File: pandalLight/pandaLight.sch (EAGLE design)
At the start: 110 parts, among them J1 PJ-037A, U13 TPD12S016PWR, U15 PMOD-2X6, U16 PMOD-2X6, U17 PLR135-T10, U18 PLT133-T10W, U20 TP10SQ, U21 TP10SQ, U22 PAN1322, U23 6SLX9TQG144, U4 FT2232HL, U5 93LC46BT-I/OT, U6 51, U7 51, U8 TPD12S016PWR, X1 USBUB-S, X2 HDMI_RECEPTICAL_A, X4 HDMI_RECEPTICAL_A, Y1 403, Y2 20Mhz

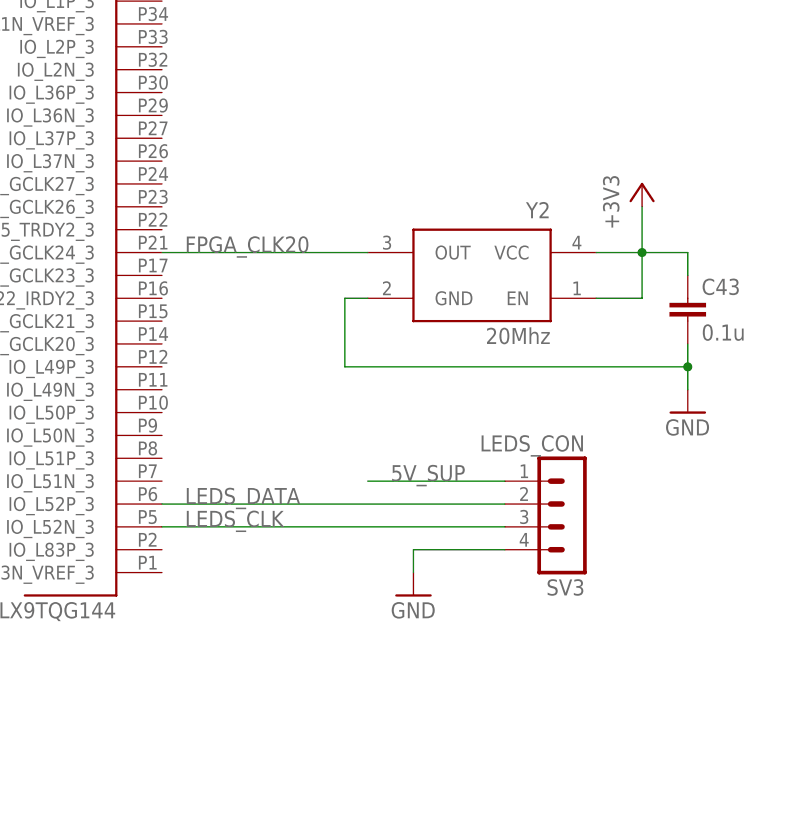
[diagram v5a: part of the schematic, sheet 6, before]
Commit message: Minor library changes; Searching for CMOS to TTL level shifters for the LED strip outputs
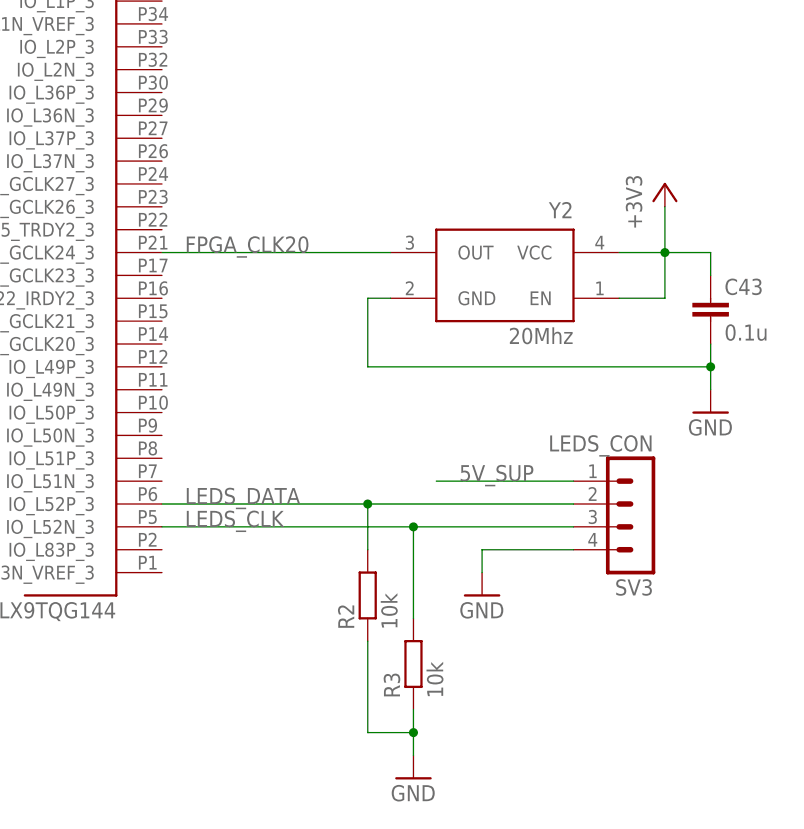
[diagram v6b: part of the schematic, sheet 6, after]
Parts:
- added R2, R3: 10k, pandaLight:RESISTOR0402
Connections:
- net GND: now also R2.1, R3.1
- net LEDS_CLK: now also R3.2
- net LEDS_DATA: now also R2.2
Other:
- moved on the sheet: C43, SV3, Y2
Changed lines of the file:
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@@
 <part name="GND7" library="pandaLight" deviceset="GND" device=""/>
 <part name="GND10" library="pandaLight" deviceset="GND" device=""/>
+<part name="R2" library="pandaLight" deviceset="RESISTOR" device="0402" value="10k"/>
+<part name="R3" library="pandaLight" deviceset="RESISTOR" device="0402" value="10k"/>
+<part name="GND16" library="pandaLight" deviceset="GND" device=""/>
 </parts>
 <sheets>
@@
 <instance part="GND46" gate="1" x="66.04" y="81.28"/>
 <instance part="U23" gate="B3" x="30.48" y="48.26"/>
-<instance part="SV3" gate="G$1" x="81.28" y="17.78" rot="R180">
-<attribute name="PARTNO" x="81.28" y="17.78" size="1.778" layer="96" display="off"/>
-<attribute name="BOM" x="81.28" y="17.78" size="1.778" layer="96" rot="R180" display="off"/>
-</instance>
-<instance part="Y2" gate="G$1" x="71.12" y="45.72" rot="MR0">
-<attribute name="PARTNO" x="71.12" y="45.72" size="1.778" layer="96" rot="MR0" display="off"/>
-</instance>
-<instance part="PS27" gate="G$1" x="88.9" y="55.88"/>
-<instance part="C43" gate="G$1" x="93.98" y="43.18">
-<attribute name="PARTNO" x="93.98" y="43.18" size="1.778" layer="96" display="off"/>
-</instance>
-<instance part="GND32" gate="1" x="93.98" y="30.48"/>
-<instance part="GND7" gate="1" x="63.5" y="10.16"/>
+<instance part="SV3" gate="G$1" x="88.9" y="17.78" rot="R180">
+<attribute name="PARTNO" x="88.9" y="17.78" size="1.778" layer="96" display="off"/>
+<attribute name="BOM" x="88.9" y="17.78" size="1.778" layer="96" rot="R180" display="off"/>
+</instance>
+<instance part="Y2" gate="G$1" x="73.66" y="45.72" rot="MR0">
+<attribute name="PARTNO" x="73.66" y="45.72" size="1.778" layer="96" rot="MR0" display="off"/>
+</instance>
+<instance part="PS27" gate="G$1" x="91.44" y="55.88"/>
+<instance part="C43" gate="G$1" x="96.52" y="43.18">
+<attribute name="PARTNO" x="96.52" y="43.18" size="1.778" layer="96" display="off"/>
+</instance>
+<instance part="GND32" gate="1" x="96.52" y="30.48"/>
+<instance part="GND7" gate="1" x="71.12" y="10.16"/>
+<instance part="R2" gate="G$1" x="58.42" y="10.16" rot="R90"/>
+<instance part="R3" gate="G$1" x="63.5" y="2.54" rot="R90"/>
+<instance part="GND16" gate="1" x="63.5" y="-10.16"/>
 </instances>
 <busses>
@@
 <pinref part="GND32" gate="1" pin="GND"/>
 <pinref part="Y2" gate="G$1" pin="GND"/>
-<wire x1="93.98" y1="35.56" x2="93.98" y2="33.02" width="0.1524" layer="91"/>
-<wire x1="58.42" y1="43.18" x2="55.88" y2="43.18" width="0.1524" layer="91"/>
-<wire x1="55.88" y1="43.18" x2="55.88" y2="35.56" width="0.1524" layer="91"/>
-<wire x1="55.88" y1="35.56" x2="93.98" y2="35.56" width="0.1524" layer="91"/>
+<wire x1="96.52" y1="35.56" x2="96.52" y2="33.02" width="0.1524" layer="91"/>
+<wire x1="60.96" y1="43.18" x2="58.42" y2="43.18" width="0.1524" layer="91"/>
+<wire x1="58.42" y1="43.18" x2="58.42" y2="35.56" width="0.1524" layer="91"/>
+<wire x1="58.42" y1="35.56" x2="96.52" y2="35.56" width="0.1524" layer="91"/>
 <pinref part="C43" gate="G$1" pin="2"/>
-<wire x1="93.98" y1="38.1" x2="93.98" y2="35.56" width="0.1524" layer="91"/>
-<junction x="93.98" y="35.56"/>
+<wire x1="96.52" y1="38.1" x2="96.52" y2="35.56" width="0.1524" layer="91"/>
+<junction x="96.52" y="35.56"/>
 </segment>
 <segment>
 <pinref part="SV3" gate="G$1" pin="4"/>
-<wire x1="73.66" y1="15.24" x2="63.5" y2="15.24" width="0.1524" layer="91"/>
-<wire x1="63.5" y1="15.24" x2="63.5" y2="12.7" width="0.1524" layer="91"/>
+<wire x1="81.28" y1="15.24" x2="71.12" y2="15.24" width="0.1524" layer="91"/>
+<wire x1="71.12" y1="15.24" x2="71.12" y2="12.7" width="0.1524" layer="91"/>
 <pinref part="GND7" gate="1" pin="GND"/>
+</segment>
+<segment>
+<pinref part="R2" gate="G$1" pin="1"/>
+<wire x1="58.42" y1="5.08" x2="58.42" y2="-5.08" width="0.1524" layer="91"/>
+<pinref part="R3" gate="G$1" pin="1"/>
+<wire x1="58.42" y1="-5.08" x2="63.5" y2="-5.08" width="0.1524" layer="91"/>
+<wire x1="63.5" y1="-5.08" x2="63.5" y2="-2.54" width="0.1524" layer="91"/>
+<pinref part="GND16" gate="1" pin="GND"/>
+<wire x1="63.5" y1="-5.08" x2="63.5" y2="-7.62" width="0.1524" layer="91"/>
+<junction x="63.5" y="-5.08"/>
 </segment>
 </net>
@@
 <pinref part="U23" gate="B3" pin="IO_L52P_3"/>
 <pinref part="SV3" gate="G$1" pin="2"/>
-<wire x1="35.56" y1="20.32" x2="73.66" y2="20.32" width="0.1524" layer="91"/>
+<wire x1="35.56" y1="20.32" x2="58.42" y2="20.32" width="0.1524" layer="91"/>
 <label x="38.1" y="20.32" size="1.778" layer="95"/>
+<pinref part="R2" gate="G$1" pin="2"/>
+<wire x1="58.42" y1="20.32" x2="81.28" y2="20.32" width="0.1524" layer="91"/>
+<wire x1="58.42" y1="20.32" x2="58.42" y2="15.24" width="0.1524" layer="91"/>
+<junction x="58.42" y="20.32"/>
 </segment>
 </net>
@@
 <pinref part="SV3" gate="G$1" pin="3"/>
 <pinref part="U23" gate="B3" pin="IO_L52N_3"/>
-<wire x1="73.66" y1="17.78" x2="35.56" y2="17.78" width="0.1524" layer="91"/>
+<wire x1="81.28" y1="17.78" x2="63.5" y2="17.78" width="0.1524" layer="91"/>
 <label x="38.1" y="17.78" size="1.778" layer="95"/>
+<wire x1="63.5" y1="17.78" x2="35.56" y2="17.78" width="0.1524" layer="91"/>
+<pinref part="R3" gate="G$1" pin="2"/>
+<wire x1="63.5" y1="17.78" x2="63.5" y2="7.62" width="0.1524" layer="91"/>
+<junction x="63.5" y="17.78"/>
 </segment>
 </net>
@@
 <pinref part="PS27" gate="G$1" pin="+3V3"/>
 <pinref part="Y2" gate="G$1" pin="VCC"/>
-<wire x1="88.9" y1="43.18" x2="88.9" y2="48.26" width="0.1524" layer="91"/>
-<wire x1="88.9" y1="48.26" x2="88.9" y2="53.34" width="0.1524" layer="91"/>
-<wire x1="83.82" y1="48.26" x2="88.9" y2="48.26" width="0.1524" layer="91"/>
-<junction x="88.9" y="48.26"/>
+<wire x1="91.44" y1="43.18" x2="91.44" y2="48.26" width="0.1524" layer="91"/>
+<wire x1="91.44" y1="48.26" x2="91.44" y2="53.34" width="0.1524" layer="91"/>
+<wire x1="86.36" y1="48.26" x2="91.44" y2="48.26" width="0.1524" layer="91"/>
+<junction x="91.44" y="48.26"/>
 <pinref part="Y2" gate="G$1" pin="EN"/>
-<wire x1="83.82" y1="43.18" x2="88.9" y2="43.18" width="0.1524" layer="91"/>
+<wire x1="86.36" y1="43.18" x2="91.44" y2="43.18" width="0.1524" layer="91"/>
 <pinref part="C43" gate="G$1" pin="1"/>
-<wire x1="88.9" y1="48.26" x2="93.98" y2="48.26" width="0.1524" layer="91"/>
-<wire x1="93.98" y1="48.26" x2="93.98" y2="45.72" width="0.1524" layer="91"/>
+<wire x1="91.44" y1="48.26" x2="96.52" y2="48.26" width="0.1524" layer="91"/>
+<wire x1="96.52" y1="48.26" x2="96.52" y2="45.72" width="0.1524" layer="91"/>
 </segment>
 </net>
@@
 <pinref part="U23" gate="B3" pin="IO_L42N_GCLK24_3"/>
 <pinref part="Y2" gate="G$1" pin="OUT"/>
-<wire x1="35.56" y1="48.26" x2="58.42" y2="48.26" width="0.1524" layer="91"/>
+<wire x1="35.56" y1="48.26" x2="60.96" y2="48.26" width="0.1524" layer="91"/>
 <label x="38.1" y="48.26" size="1.778" layer="95"/>
 </segment>
@@
 <segment>
 <pinref part="SV3" gate="G$1" pin="1"/>
-<wire x1="73.66" y1="22.86" x2="58.42" y2="22.86" width="0.1524" layer="91"/>
-<label x="60.96" y="22.86" size="1.778" layer="95"/>
-</segment>
-</net>
+<wire x1="81.28" y1="22.86" x2="66.04" y2="22.86" width="0.1524" layer="91"/>
+<label x="68.58" y="22.86" size="1.778" layer="95"/>
+</segment>
+</net>

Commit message: Minor changes; Still looking for decent pin protection
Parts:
- added R4, R6: 200, pandaLight:RESISTOR0402
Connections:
- new net N$2: R2.2, R4.2, SV3.2
- new net N$3: R3.2, R6.2, SV3.3
- net LEDS_CLK: now also R6.1; no longer R3.2, SV3.3
- net LEDS_DATA: now also R4.1; no longer R2.2, SV3.2
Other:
- note added: "1.2V, 0.8A"
- note added: "3.3V, 0.8A"
- note removed: "1.2V, 0.6A"
- note removed: "3.3V, 0.6A"
- moved on the sheet: C43, R2, R3, SV3, Y2
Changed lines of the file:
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@@
 <part name="R3" library="pandaLight" deviceset="RESISTOR" device="0402" value="10k"/>
 <part name="GND16" library="pandaLight" deviceset="GND" device=""/>
+<part name="R4" library="pandaLight" deviceset="RESISTOR" device="0402" value="200"/>
+<part name="R6" library="pandaLight" deviceset="RESISTOR" device="0402" value="200"/>
 </parts>
 <sheets>
@@
 <plain>
 <text x="22.86" y="96.52" size="2.54" layer="97">4.5V - 5.5V, 2A</text>
-<text x="119.38" y="48.26" size="2.54" layer="97">3.3V, 0.6A</text>
-<text x="119.38" y="33.02" size="2.54" layer="97">1.2V, 0.6A</text>
+<text x="119.38" y="48.26" size="2.54" layer="97">3.3V, 0.8A</text>
+<text x="119.38" y="33.02" size="2.54" layer="97">1.2V, 0.8A</text>
 </plain>
 <instances>
@@
 <instance part="GND46" gate="1" x="66.04" y="81.28"/>
 <instance part="U23" gate="B3" x="30.48" y="48.26"/>
-<instance part="SV3" gate="G$1" x="88.9" y="17.78" rot="R180">
-<attribute name="PARTNO" x="88.9" y="17.78" size="1.778" layer="96" display="off"/>
-<attribute name="BOM" x="88.9" y="17.78" size="1.778" layer="96" rot="R180" display="off"/>
-</instance>
-<instance part="Y2" gate="G$1" x="73.66" y="45.72" rot="MR0">
-<attribute name="PARTNO" x="73.66" y="45.72" size="1.778" layer="96" rot="MR0" display="off"/>
-</instance>
-<instance part="PS27" gate="G$1" x="91.44" y="55.88"/>
-<instance part="C43" gate="G$1" x="96.52" y="43.18">
-<attribute name="PARTNO" x="96.52" y="43.18" size="1.778" layer="96" display="off"/>
-</instance>
-<instance part="GND32" gate="1" x="96.52" y="30.48"/>
-<instance part="GND7" gate="1" x="71.12" y="10.16"/>
-<instance part="R2" gate="G$1" x="58.42" y="10.16" rot="R90"/>
-<instance part="R3" gate="G$1" x="63.5" y="2.54" rot="R90"/>
-<instance part="GND16" gate="1" x="63.5" y="-10.16"/>
+<instance part="SV3" gate="G$1" x="114.3" y="17.78" rot="R180">
+<attribute name="PARTNO" x="114.3" y="17.78" size="1.778" layer="96" display="off"/>
+<attribute name="BOM" x="114.3" y="17.78" size="1.778" layer="96" rot="R180" display="off"/>
+</instance>
+<instance part="Y2" gate="G$1" x="76.2" y="53.34" rot="MR0">
+<attribute name="PARTNO" x="76.2" y="53.34" size="1.778" layer="96" rot="MR0" display="off"/>
+</instance>
+<instance part="PS27" gate="G$1" x="93.98" y="63.5"/>
+<instance part="C43" gate="G$1" x="99.06" y="50.8">
+<attribute name="PARTNO" x="99.06" y="50.8" size="1.778" layer="96" display="off"/>
+</instance>
+<instance part="GND32" gate="1" x="99.06" y="38.1"/>
+<instance part="GND7" gate="1" x="96.52" y="10.16"/>
+<instance part="R2" gate="G$1" x="81.28" y="10.16" rot="R90"/>
+<instance part="R3" gate="G$1" x="86.36" y="2.54" rot="R90"/>
+<instance part="GND16" gate="1" x="86.36" y="-10.16"/>
+<instance part="R4" gate="G$1" x="60.96" y="20.32"/>
+<instance part="R6" gate="G$1" x="68.58" y="15.24"/>
 </instances>
 <busses>
@@
 <pinref part="GND32" gate="1" pin="GND"/>
 <pinref part="Y2" gate="G$1" pin="GND"/>
-<wire x1="96.52" y1="35.56" x2="96.52" y2="33.02" width="0.1524" layer="91"/>
-<wire x1="60.96" y1="43.18" x2="58.42" y2="43.18" width="0.1524" layer="91"/>
-<wire x1="58.42" y1="43.18" x2="58.42" y2="35.56" width="0.1524" layer="91"/>
-<wire x1="58.42" y1="35.56" x2="96.52" y2="35.56" width="0.1524" layer="91"/>
+<wire x1="99.06" y1="43.18" x2="99.06" y2="40.64" width="0.1524" layer="91"/>
+<wire x1="63.5" y1="50.8" x2="60.96" y2="50.8" width="0.1524" layer="91"/>
+<wire x1="60.96" y1="50.8" x2="60.96" y2="43.18" width="0.1524" layer="91"/>
+<wire x1="60.96" y1="43.18" x2="99.06" y2="43.18" width="0.1524" layer="91"/>
 <pinref part="C43" gate="G$1" pin="2"/>
-<wire x1="96.52" y1="38.1" x2="96.52" y2="35.56" width="0.1524" layer="91"/>
-<junction x="96.52" y="35.56"/>
+<wire x1="99.06" y1="45.72" x2="99.06" y2="43.18" width="0.1524" layer="91"/>
+<junction x="99.06" y="43.18"/>
 </segment>
 <segment>
 <pinref part="SV3" gate="G$1" pin="4"/>
-<wire x1="81.28" y1="15.24" x2="71.12" y2="15.24" width="0.1524" layer="91"/>
-<wire x1="71.12" y1="15.24" x2="71.12" y2="12.7" width="0.1524" layer="91"/>
+<wire x1="106.68" y1="15.24" x2="96.52" y2="15.24" width="0.1524" layer="91"/>
+<wire x1="96.52" y1="15.24" x2="96.52" y2="12.7" width="0.1524" layer="91"/>
 <pinref part="GND7" gate="1" pin="GND"/>
 </segment>
 <segment>
 <pinref part="R2" gate="G$1" pin="1"/>
-<wire x1="58.42" y1="5.08" x2="58.42" y2="-5.08" width="0.1524" layer="91"/>
+<wire x1="81.28" y1="5.08" x2="81.28" y2="-5.08" width="0.1524" layer="91"/>
 <pinref part="R3" gate="G$1" pin="1"/>
-<wire x1="58.42" y1="-5.08" x2="63.5" y2="-5.08" width="0.1524" layer="91"/>
-<wire x1="63.5" y1="-5.08" x2="63.5" y2="-2.54" width="0.1524" layer="91"/>
+<wire x1="81.28" y1="-5.08" x2="86.36" y2="-5.08" width="0.1524" layer="91"/>
+<wire x1="86.36" y1="-5.08" x2="86.36" y2="-2.54" width="0.1524" layer="91"/>
 <pinref part="GND16" gate="1" pin="GND"/>
-<wire x1="63.5" y1="-5.08" x2="63.5" y2="-7.62" width="0.1524" layer="91"/>
-<junction x="63.5" y="-5.08"/>
+<wire x1="86.36" y1="-5.08" x2="86.36" y2="-7.62" width="0.1524" layer="91"/>
+<junction x="86.36" y="-5.08"/>
 </segment>
 </net>
@@
 <segment>
 <pinref part="U23" gate="B3" pin="IO_L52P_3"/>
-<pinref part="SV3" gate="G$1" pin="2"/>
-<wire x1="35.56" y1="20.32" x2="58.42" y2="20.32" width="0.1524" layer="91"/>
+<wire x1="35.56" y1="20.32" x2="55.88" y2="20.32" width="0.1524" layer="91"/>
 <label x="38.1" y="20.32" size="1.778" layer="95"/>
-<pinref part="R2" gate="G$1" pin="2"/>
-<wire x1="58.42" y1="20.32" x2="81.28" y2="20.32" width="0.1524" layer="91"/>
-<wire x1="58.42" y1="20.32" x2="58.42" y2="15.24" width="0.1524" layer="91"/>
-<junction x="58.42" y="20.32"/>
+<pinref part="R4" gate="G$1" pin="1"/>
 </segment>
 </net>
 <net name="LEDS_CLK" class="0">
 <segment>
-<pinref part="SV3" gate="G$1" pin="3"/>
 <pinref part="U23" gate="B3" pin="IO_L52N_3"/>
-<wire x1="81.28" y1="17.78" x2="63.5" y2="17.78" width="0.1524" layer="91"/>
 <label x="38.1" y="17.78" size="1.778" layer="95"/>
-<wire x1="63.5" y1="17.78" x2="35.56" y2="17.78" width="0.1524" layer="91"/>
-<pinref part="R3" gate="G$1" pin="2"/>
-<wire x1="63.5" y1="17.78" x2="63.5" y2="7.62" width="0.1524" layer="91"/>
-<junction x="63.5" y="17.78"/>
+<wire x1="53.34" y1="17.78" x2="35.56" y2="17.78" width="0.1524" layer="91"/>
+<wire x1="53.34" y1="17.78" x2="53.34" y2="15.24" width="0.1524" layer="91"/>
+<pinref part="R6" gate="G$1" pin="1"/>
+<wire x1="53.34" y1="15.24" x2="63.5" y2="15.24" width="0.1524" layer="91"/>
 </segment>
 </net>
@@
 <pinref part="PS27" gate="G$1" pin="+3V3"/>
 <pinref part="Y2" gate="G$1" pin="VCC"/>
-<wire x1="91.44" y1="43.18" x2="91.44" y2="48.26" width="0.1524" layer="91"/>
-<wire x1="91.44" y1="48.26" x2="91.44" y2="53.34" width="0.1524" layer="91"/>
-<wire x1="86.36" y1="48.26" x2="91.44" y2="48.26" width="0.1524" layer="91"/>
-<junction x="91.44" y="48.26"/>
+<wire x1="93.98" y1="50.8" x2="93.98" y2="55.88" width="0.1524" layer="91"/>
+<wire x1="93.98" y1="55.88" x2="93.98" y2="60.96" width="0.1524" layer="91"/>
+<wire x1="88.9" y1="55.88" x2="93.98" y2="55.88" width="0.1524" layer="91"/>
+<junction x="93.98" y="55.88"/>
 <pinref part="Y2" gate="G$1" pin="EN"/>
-<wire x1="86.36" y1="43.18" x2="91.44" y2="43.18" width="0.1524" layer="91"/>
+<wire x1="88.9" y1="50.8" x2="93.98" y2="50.8" width="0.1524" layer="91"/>
 <pinref part="C43" gate="G$1" pin="1"/>
-<wire x1="91.44" y1="48.26" x2="96.52" y2="48.26" width="0.1524" layer="91"/>
-<wire x1="96.52" y1="48.26" x2="96.52" y2="45.72" width="0.1524" layer="91"/>
+<wire x1="93.98" y1="55.88" x2="99.06" y2="55.88" width="0.1524" layer="91"/>
+<wire x1="99.06" y1="55.88" x2="99.06" y2="53.34" width="0.1524" layer="91"/>
 </segment>
 </net>
@@
 <pinref part="U23" gate="B3" pin="IO_L42N_GCLK24_3"/>
 <pinref part="Y2" gate="G$1" pin="OUT"/>
-<wire x1="35.56" y1="48.26" x2="60.96" y2="48.26" width="0.1524" layer="91"/>
+<wire x1="35.56" y1="48.26" x2="58.42" y2="48.26" width="0.1524" layer="91"/>
+<wire x1="58.42" y1="48.26" x2="58.42" y2="55.88" width="0.1524" layer="91"/>
+<wire x1="58.42" y1="55.88" x2="63.5" y2="55.88" width="0.1524" layer="91"/>
 <label x="38.1" y="48.26" size="1.778" layer="95"/>
 </segment>
@@
 <segment>
 <pinref part="SV3" gate="G$1" pin="1"/>
-<wire x1="81.28" y1="22.86" x2="66.04" y2="22.86" width="0.1524" layer="91"/>
-<label x="68.58" y="22.86" size="1.778" layer="95"/>
-</segment>
-</net>
+<wire x1="106.68" y1="22.86" x2="91.44" y2="22.86" width="0.1524" layer="91"/>
+<label x="93.98" y="22.86" size="1.778" layer="95"/>
+</segment>
+</net>
+<net name="N$2" class="0">
+<segment>
+<pinref part="R4" gate="G$1" pin="2"/>
+<pinref part="SV3" gate="G$1" pin="2"/>
+<wire x1="66.04" y1="20.32" x2="81.28" y2="20.32" width="0.1524" layer="91"/>
+<pinref part="R2" gate="G$1" pin="2"/>
+<wire x1="81.28" y1="20.32" x2="106.68" y2="20.32" width="0.1524" layer="91"/>
+<wire x1="81.28" y1="15.24" x2="81.28" y2="20.32" width="0.1524" layer="91"/>
+<junction x="81.28" y="20.32"/>
+</segment>
+</net>
+<net name="N$3" class="0">
+<segment>
+<pinref part="SV3" gate="G$1" pin="3"/>
+<wire x1="106.68" y1="17.78" x2="86.36" y2="17.78" width="0.1524" layer="91"/>
+<wire x1="86.36" y1="17.78" x2="76.2" y2="17.78" width="0.1524" layer="91"/>
+<wire x1="76.2" y1="17.78" x2="76.2" y2="15.24" width="0.1524" layer="91"/>
+<pinref part="R6" gate="G$1" pin="2"/>
+<wire x1="76.2" y1="15.24" x2="73.66" y2="15.24" width="0.1524" layer="91"/>
+<pinref part="R3" gate="G$1" pin="2"/>
+<wire x1="86.36" y1="17.78" x2="86.36" y2="7.62" width="0.1524" layer="91"/>
+<junction x="86.36" y="17.78"/>
+</segment>
+</net>
